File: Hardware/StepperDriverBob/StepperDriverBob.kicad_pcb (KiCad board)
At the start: 2 copper layers, 20 parts, among them P1 CONN_01X02, P3 CONN_01X09, P4 CONN_01X04, U1 DRV8825

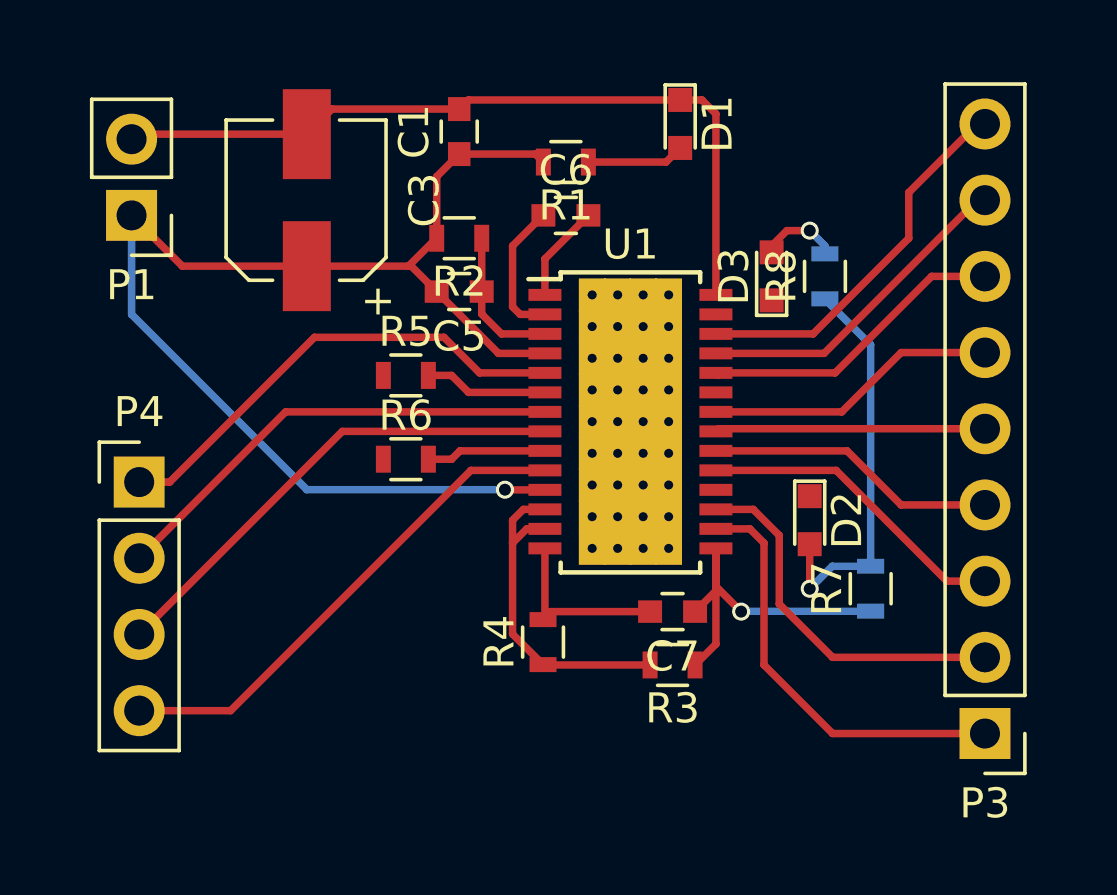
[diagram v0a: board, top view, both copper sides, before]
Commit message: Finished pcb layout
-drv8825.lib connected thermal pad to ground
-changed global labels to local labels for readability
-finsihed routing pcb(just need to do ground plane.
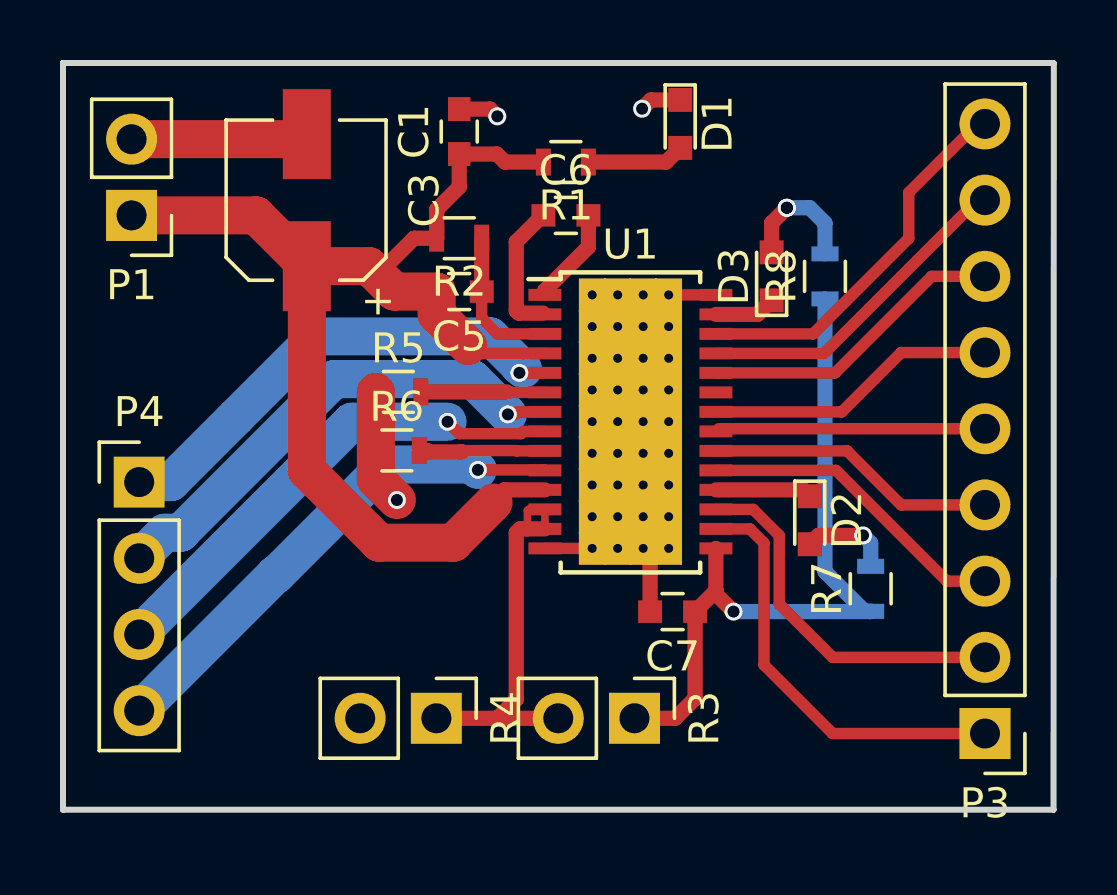
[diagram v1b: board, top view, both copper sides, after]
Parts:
- D2: value nFAULT -> ~FAULT~
- D3: value nHOME -> ~HOME~
- R3: footprint Resistors_SMD:R_0603 -> Pin_Headers:Pin_Header_Straight_1x02_Pitch2.54mm
- R4: value 50k -> 30k; footprint Resistors_SMD:R_0603 -> Pin_Headers:Pin_Header_Straight_1x02_Pitch2.54mm
- moved R4 4.37 mm to (140.7, 94.0), turned to 270 degrees
- moved R3 2.18 mm to (147.3, 94.0), turned to 270 degrees
- moved R5 0.60 mm to (139.4, 83.1)
- moved R6 0.42 mm to (139.4, 85.0)
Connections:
- net AOUT1 renamed /AOUT1
- net AOUT2 renamed /A0UT2
- net BOUT1 renamed /BOUT1
- net BOUT2 renamed /BOUT2
- net DECAY renamed /DECAY
- net DIR renamed /DIR
- net MODE0 renamed /MODE0
- net MODE1 renamed /MODE1
- net MODE2 renamed /MODE2
- net STEP renamed /STEP
- net nENBL renamed /~ENBL~
- net nSLEEP renamed /~SLEEP~
- net ~nRESET~ renamed /~RST~
- D2 pad 1: nFAULT -> /~FAULT~
- D3 pad 1: nHOME -> /~HOME~
- U1 pad 18: ~nFAULT~ -> /~FAULT~
- U1 pad 27: ~nHOME~ -> /~HOME~
- U1 pad 29: (no net) -> GND
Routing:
- net GND: track 32.1 -> 18.2 mm, vias 0 -> 3
- net +3V3: track 14.2 -> 24.3 mm
- net Net-(D2-Pad2): track 11.2 -> 3.03 mm
- net /~FAULT~: track 0.00 -> 3.21 mm
- net Net-(R3-Pad2): track 11.3 -> 13.4 mm
- net /~HOME~: track 0.00 -> 2.05 mm
- net Net-(D3-Pad2): track 2.68 -> 4.42 mm, vias 1 -> 2
- net VDD: track 43.3 -> 41.6 mm, vias 1 -> 0
- net /A0UT2: track 15.5 -> 16.5 mm, vias 0 -> 1
- net /BOUT2: track 16.3 -> 16.7 mm, vias 0 -> 1
- net /BOUT1: track 16.8 -> 17.0 mm, vias 0 -> 1
- net /AOUT1: track 16.0 -> 16.1 mm, vias 0 -> 1
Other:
- board outline added: 33 x 24.9 mm
- net class Default: clearance 0.2 -> 0.1524; trace_width 0.25 -> 0.1524
- rule trace_clearance: 0.2 -> 0.1524
- rule trace_min: 0.2 -> 0.1524

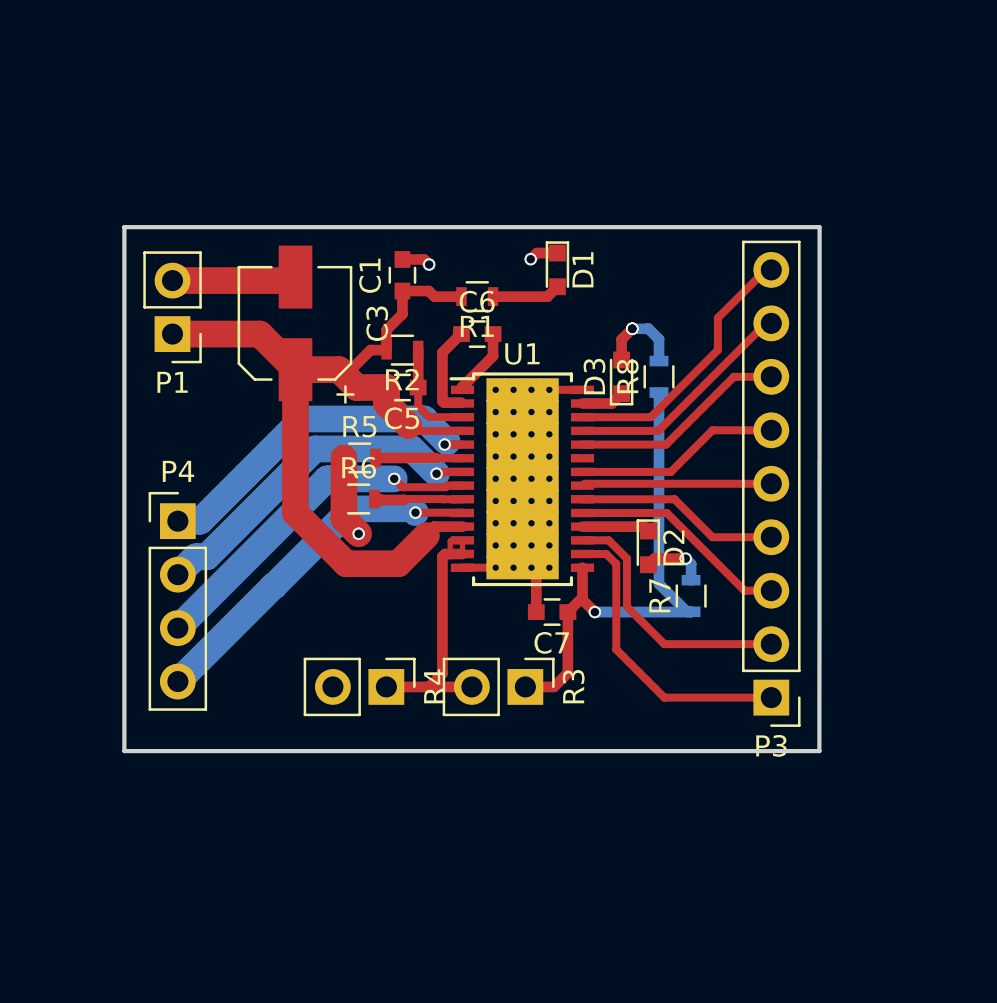
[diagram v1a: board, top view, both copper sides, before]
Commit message: Finished up pcb routing
+Holdes for standoffs
+Made the board larger 1.7x.1.7 in
+Rerouted entire board
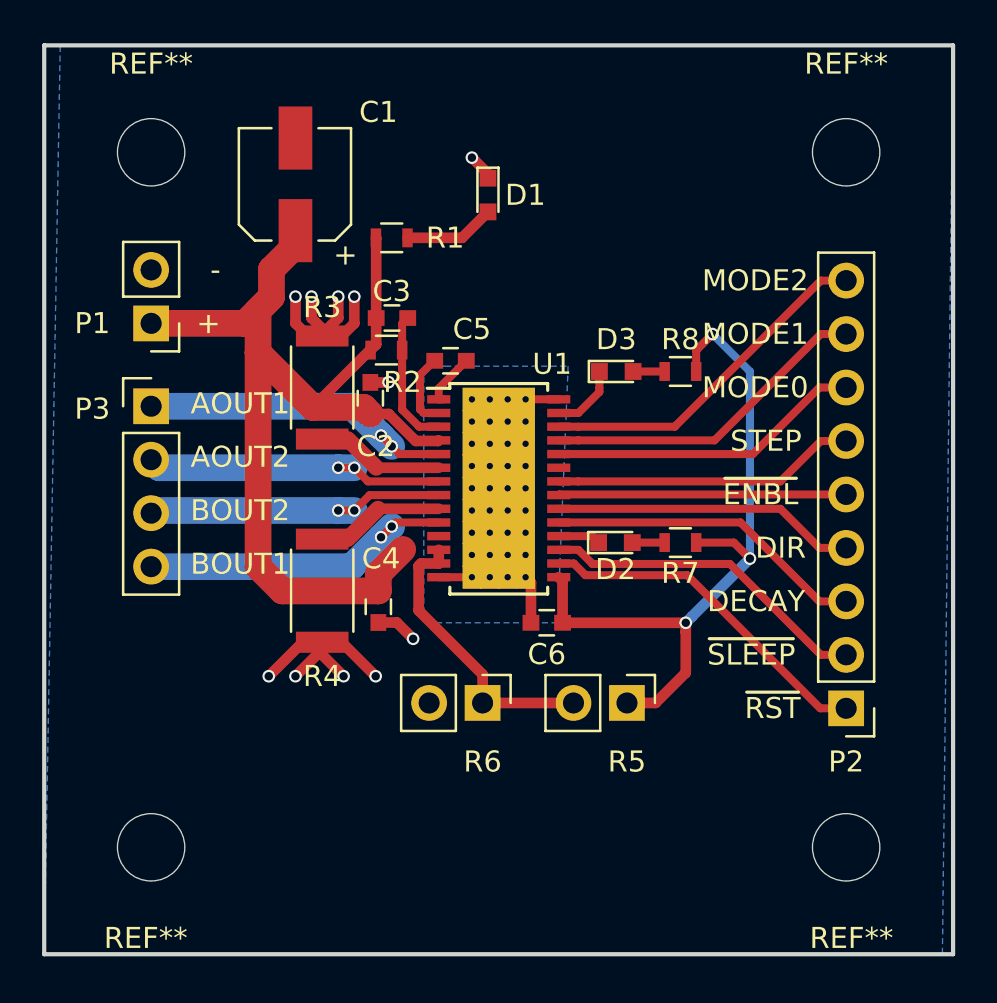
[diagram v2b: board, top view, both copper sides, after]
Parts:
- removed C7: 470nF, Capacitors_SMD:C_0603
- removed P4: CONN_01X04, Pin_Headers:Pin_Header_Straight_1x04_Pitch2.54mm
- added C2: 100nF, Capacitors_SMD:C_0603, F.Cu at (140.0, 80.3)
- added C4: 100nF, Capacitors_SMD:C_0603, F.Cu at (140.3, 90.2)
- added P2: CONN_01X09, Pin_Headers:Pin_Header_Straight_1x09_Pitch2.54mm, F.Cu at (162.6, 95.0)
- added REF**: MountingHole_3.2mm_M3, Mounting_Holes:MountingHole_3.2mm_M3, F.Cu at (129.5, 101.6)
- added REF**: MountingHole_3.2mm_M3, Mounting_Holes:MountingHole_3.2mm_M3, F.Cu at (129.5, 68.6)
- added REF**: MountingHole_3.2mm_M3, Mounting_Holes:MountingHole_3.2mm_M3, F.Cu at (162.6, 68.6)
- added REF**: MountingHole_3.2mm_M3, Mounting_Holes:MountingHole_3.2mm_M3, F.Cu at (162.6, 101.6)
- C1: value 100nF -> 100uF; footprint Capacitors_SMD:C_0603 -> Capacitors_SMD:CP_Elec_5x5.3
- C3: value 100uF -> 100nF; footprint Capacitors_SMD:CP_Elec_5x5.3 -> Capacitors_SMD:C_0603
- C5: value 100nF -> 10nF
- C6: value 10nF -> 470nF
- P3: value CONN_01X09 -> CONN_01X04; footprint Pin_Headers:Pin_Header_Straight_1x09_Pitch2.54mm -> Pin_Headers:Pin_Header_Straight_1x04_Pitch2.54mm
- R3: value 50k -> .2R; footprint Pin_Headers:Pin_Header_Straight_1x02_Pitch2.54mm -> Resistors_SMD:R_2010
- R4: value 30k -> .2R; footprint Pin_Headers:Pin_Header_Straight_1x02_Pitch2.54mm -> Resistors_SMD:R_2010
- R5, R6: value .2R -> 50k; footprint Resistors_SMD:R_0603 -> Pin_Headers:Pin_Header_Straight_1x02_Pitch2.54mm
- moved P3 32.6 mm to (129.5, 80.6), turned to 0 degrees
- moved R5 17.2 mm to (152.1, 94.7), turned to 270 degrees
- moved R3 17.2 mm to (137.7, 79.8)
- moved C6 14.1 mm to (148.3, 90.9), turned to 180 degrees
- moved R6 11.3 mm to (145.3, 94.7), turned to 270 degrees
- moved C1 6.67 mm to (136.4, 70.1)
- moved R4 5.49 mm to (137.7, 89.4), turned to 90 degrees
- moved R1 4.93 mm to (141.0, 72.6)
- moved D1 4.85 mm to (145.5, 70.6)
- moved C3 4.59 mm to (141.0, 76.5), turned to 180 degrees
- moved C5 2.62 mm to (143.8, 78.5), turned to 0 degrees
- moved R7 2.59 mm to (154.7, 87.1), turned to 180 degrees
- moved D2 1.58 mm to (151.6, 87.1), turned to 0 degrees
- moved U1 1.22 mm to (146.1, 84.5)
- moved P1 1.14 mm to (129.5, 76.7)
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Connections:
- C3 pad 1: VDD -> Net-(C3-Pad1)
- C3 pad 2: GND -> VDD
- C5 pad 2: VDD -> Net-(C5-Pad2)
- C6 pad 1: Net-(C6-Pad1) -> +3V3
- C6 pad 2: Net-(C6-Pad2) -> GND
- P3 pad 1: /~RST~ -> /AOUT1
- P3 pad 2: /~SLEEP~ -> /A0UT2
- P3 pad 3: /DECAY -> /BOUT2
- P3 pad 4: /DIR -> /BOUT1
- R2 pad 1: Net-(C5-Pad1) -> Net-(C3-Pad1)
- R3 pad 1: +3V3 -> GND
- R4 pad 1: Net-(R3-Pad2) -> GND
- R4 pad 2: GND -> Net-(R4-Pad2)
- R5 pad 1: GND -> +3V3
- R6 pad 1: GND -> Net-(R5-Pad2)
- R6 pad 2: Net-(R6-Pad2) -> GND
- U1 pad 1: Net-(C6-Pad2) -> Net-(C5-Pad2)
- U1 pad 12: Net-(R3-Pad2) -> Net-(R5-Pad2)
- U1 pad 13: Net-(R3-Pad2) -> Net-(R5-Pad2)
- U1 pad 2: Net-(C6-Pad1) -> Net-(C5-Pad1)
- U1 pad 3: Net-(C5-Pad1) -> Net-(C3-Pad1)
- U1 pad 6: Net-(R5-Pad2) -> Net-(R3-Pad2)
- U1 pad 9: Net-(R6-Pad2) -> Net-(R4-Pad2)
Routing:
- net GND: track 18.2 -> 30.4 mm, vias 3 -> 11
- net +3V3: track 24.3 -> 34.5 mm, vias 1 -> 3
- net VDD: track 41.6 -> 51.6 mm
- net Net-(R5-Pad2): track 4.14 -> 13.9 mm
- net Net-(R3-Pad2): track 13.4 -> 6.10 mm
- net Net-(C3-Pad1): track 0.00 -> 6.54 mm
- net Net-(R4-Pad2): track 0.00 -> 6.13 mm
- net /DIR: track 9.72 -> 14.4 mm
- net /DECAY: track 10.5 -> 15.2 mm
- net /~ENBL~: track 9.01 -> 13.7 mm
- net /STEP: track 9.86 -> 14.5 mm
- net Net-(C6-Pad1): track 4.50 -> 0.00 mm
- net Net-(R6-Pad2): track 4.23 -> 0.00 mm
- net /MODE1: track 11.6 -> 15.7 mm
- net /MODE0: track 10.9 -> 15.0 mm
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- added copper zone on B.Cu, net GND
- added copper zone on F.Cu, net GND
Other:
- board size 33 x 24.9 mm -> 43.2 x 43.2 mm
- board text added: "+"
- board text added: "-"
- board text added: "AOUT1"
- board text added: "AOUT2"
- board text added: "BOUT1"
- board text added: "BOUT2"
- board text added: "DECAY"
- board text added: "DIR"
- board text added: "MODE0"
- board text added: "MODE1"
- board text added: "MODE2"
- board text added: "STEP"
- board text added: "~ENBL~"
- board text added: "~RST~"
- board text added: "~SLEEP~"

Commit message: Added pins for fault and home outpouts
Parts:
- removed P3: CONN_01X04, Pin_Headers:Pin_Header_Straight_1x04_Pitch2.54mm
- removed REF** (x4): MountingHole_3.2mm_M3, Mounting_Holes:MountingHole_3.2mm_M3
- added J1: CONN_01X11, Pin_Headers:Pin_Header_Straight_1x11_Pitch2.54mm, F.Cu at (162.6, 97.5)
- P2: value CONN_01X09 -> CONN_01X04; footprint Pin_Headers:Pin_Header_Straight_1x09_Pitch2.54mm -> Pin_Headers:Pin_Header_Straight_1x04_Pitch2.54mm
- moved P2 36.1 mm to (129.5, 80.5), turned to 0 degrees
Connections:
- P2 pad 1: /~RST~ -> /AOUT1
- P2 pad 2: /~SLEEP~ -> /A0UT2
- P2 pad 3: /DECAY -> /BOUT2
- P2 pad 4: /DIR -> /BOUT1
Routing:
- net /~HOME~: track 3.32 -> 18.3 mm
- net /~FAULT~: track 2.02 -> 16.0 mm
- net /~RST~: track 16.5 -> 18.3 mm
- net /~SLEEP~: track 15.7 -> 16.8 mm
- net +3V3: track 34.5 -> 33.5 mm

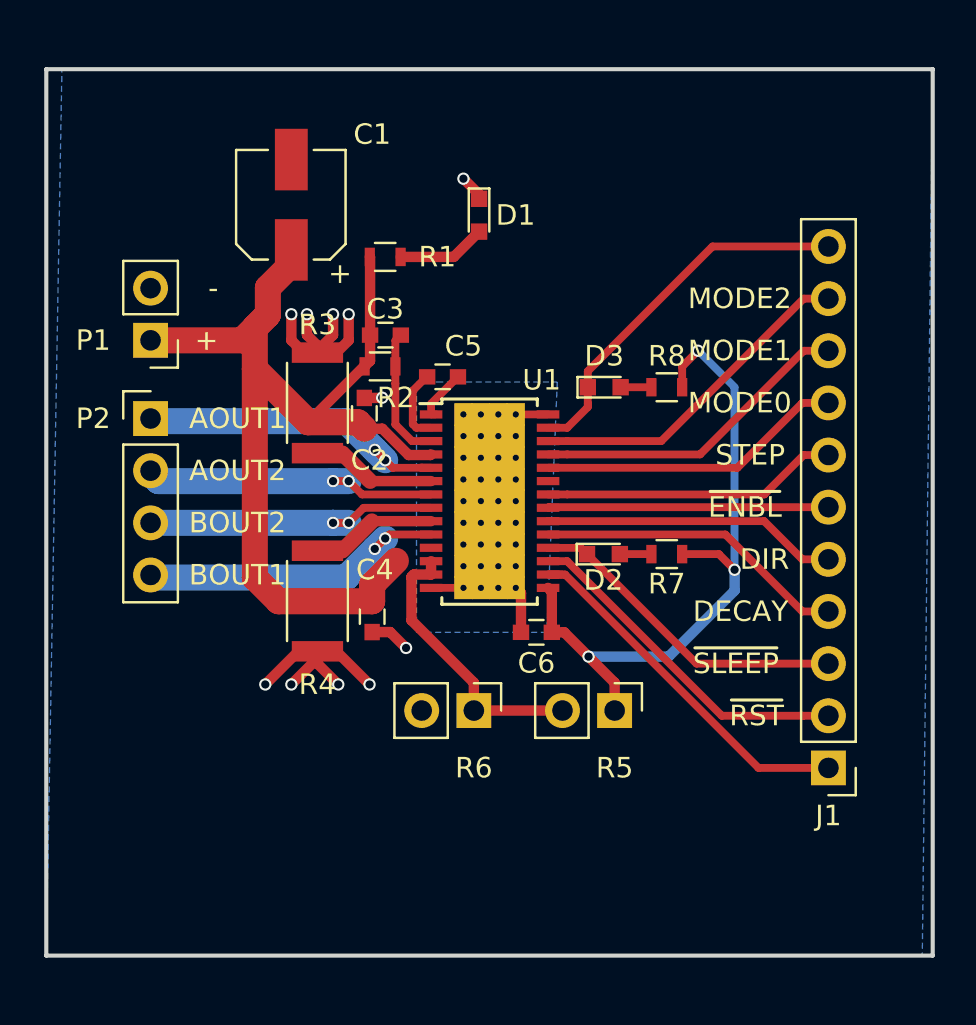
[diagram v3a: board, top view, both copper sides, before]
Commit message: Finishing Touches
+added holes for offset in schmatic so they wouldn't disspear upon
reloading netlist
+added through holdes to make sure ground planes are connected
+updated silkscreen labels
+moved some components around so that silk screen labels identified them
more easily
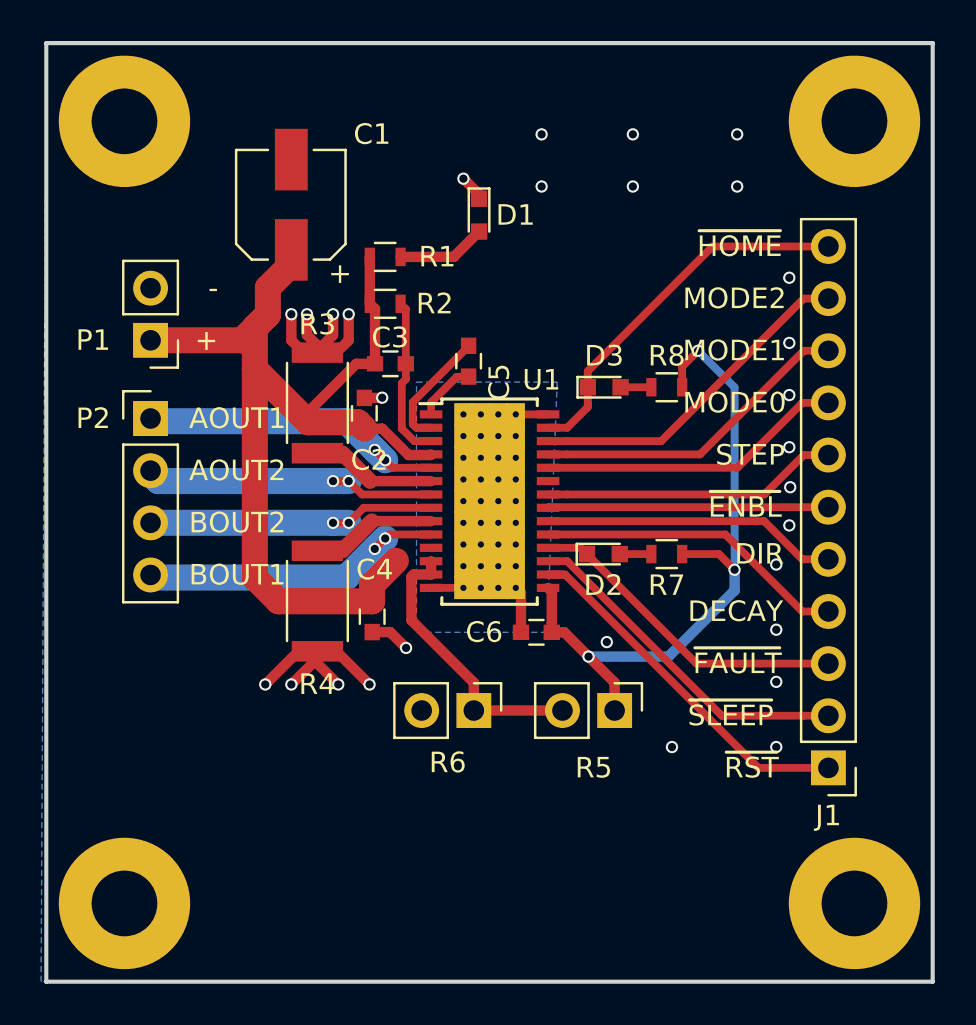
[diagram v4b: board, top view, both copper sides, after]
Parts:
- added ?: MOUNT1, Mounting_Holes:MountingHole_3.2mm_M3_Pad, F.Cu at (128.3, 66.0)
- added ?: MOUNT2, Mounting_Holes:MountingHole_3.2mm_M3_Pad, F.Cu at (163.8, 66.0)
- added ?: MOUNT3, Mounting_Holes:MountingHole_3.2mm_M3_Pad, F.Cu at (163.8, 104.1)
- added ?: MOUNT4, Mounting_Holes:MountingHole_3.2mm_M3_Pad, F.Cu at (128.3, 104.1)
- moved R2 3.06 mm to (141.0, 74.9)
- moved C5 1.48 mm to (145.0, 77.7), turned to 270 degrees
- moved C3 1.42 mm to (141.2, 77.9)
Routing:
- net Net-(C5-Pad1): track 3.58 -> 5.91 mm
- net Net-(C3-Pad1): track 6.54 -> 7.94 mm
- net VDD: track 51.6 -> 52.3 mm
- net GND: track 30.4 -> 30.7 mm, vias 11 -> 29
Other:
- board size 43.2 x 43.2 mm -> 43.2 x 45.7 mm
- board text added: "~FAULT~"
- board text added: "~HOME~"
